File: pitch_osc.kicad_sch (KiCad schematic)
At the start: 32 parts, among them Q1 2N3904, Q2 2N3904, Q3 2N3904, Q4 2N3904, Q5 2N3904

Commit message: Placed in smd and through.
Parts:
- C1, C2, C3, C5, C6, C7, C9: footprint Capacitor_THT:C_Disc_D11.0mm_W5.0mm_P7.50mm -> Capacitor_SMD:C_0805_2012Metric
- C10, C11, C4, C8: footprint Capacitor_THT:CP_Radial_D10.0mm_P3.80mm -> Capacitor_THT:CP_Radial_D5.0mm_P2.50mm
- L5, L6: footprint Inductor_THT:L_Axial_L7.0mm_D3.3mm_P12.70mm_Horizontal_Fastron_MICC -> Inductor_SMD:L_1210_3225Metric
- R1, R10, R11, R12, R13, R14, R2, R3, R4, R5, R6, R7, R8, R9: footprint Resistor_THT:R_Axial_DIN0207_L6.3mm_D2.5mm_P10.16mm_Horizontal -> Resistor_SMD:R_0805_2012Metric
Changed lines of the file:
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@@
       (effects (font (size 1.27 1.27)) (justify left))
     )
-    (property "Footprint" "Resistor_THT:R_Axial_DIN0207_L6.3mm_D2.5mm_P10.16mm_Horizontal" (at 180.086 100.584 90)
+    (property "Footprint" "Resistor_SMD:R_0805_2012Metric" (at 180.086 100.584 90)
       (effects (font (size 1.27 1.27)) hide)
     )
@@
       (effects (font (size 1.27 1.27)) (justify left))
     )
-    (property "Footprint" "Resistor_THT:R_Axial_DIN0207_L6.3mm_D2.5mm_P10.16mm_Horizontal" (at 219.456 104.394 90)
+    (property "Footprint" "Resistor_SMD:R_0805_2012Metric" (at 219.456 104.394 90)
       (effects (font (size 1.27 1.27)) hide)
     )
@@
       (effects (font (size 1.27 1.27)) (justify left))
     )
-    (property "Footprint" "Resistor_THT:R_Axial_DIN0207_L6.3mm_D2.5mm_P10.16mm_Horizontal" (at 105.156 99.314 90)
+    (property "Footprint" "Resistor_SMD:R_0805_2012Metric" (at 105.156 99.314 90)
       (effects (font (size 1.27 1.27)) hide)
     )
@@
       (effects (font (size 1.27 1.27)) (justify left))
     )
-    (property "Footprint" "Resistor_THT:R_Axial_DIN0207_L6.3mm_D2.5mm_P10.16mm_Horizontal" (at 180.086 87.884 90)
+    (property "Footprint" "Resistor_SMD:R_0805_2012Metric" (at 180.086 87.884 90)
       (effects (font (size 1.27 1.27)) hide)
     )
@@
       (effects (font (size 1.27 1.27)) (justify left))
     )
-    (property "Footprint" "Resistor_THT:R_Axial_DIN0207_L6.3mm_D2.5mm_P10.16mm_Horizontal" (at 141.986 101.854 90)
+    (property "Footprint" "Resistor_SMD:R_0805_2012Metric" (at 141.986 101.854 90)
       (effects (font (size 1.27 1.27)) hide)
     )
@@
       (effects (font (size 1.27 1.27)) (justify left))
     )
-    (property "Footprint" "Inductor_THT:L_Axial_L7.0mm_D3.3mm_P12.70mm_Horizontal_Fastron_MICC" (at 147.32 72.39 0)
+    (property "Footprint" "Inductor_SMD:L_1210_3225Metric" (at 147.32 72.39 0)
       (effects (font (size 1.27 1.27)) hide)
     )
@@
       (effects (font (size 1.27 1.27)) (justify left))
     )
-    (property "Footprint" "Resistor_THT:R_Axial_DIN0207_L6.3mm_D2.5mm_P10.16mm_Horizontal" (at 105.156 90.424 90)
+    (property "Footprint" "Resistor_SMD:R_0805_2012Metric" (at 105.156 90.424 90)
       (effects (font (size 1.27 1.27)) hide)
     )
@@
       (effects (font (size 1.27 1.27)) (justify left))
     )
-    (property "Footprint" "Capacitor_THT:CP_Radial_D10.0mm_P3.80mm" (at 201.6252 97.79 0)
+    (property "Footprint" "Capacitor_THT:CP_Radial_D5.0mm_P2.50mm" (at 201.6252 97.79 0)
       (effects (font (size 1.27 1.27)) hide)
     )
@@
       (effects (font (size 1.27 1.27)) (justify right))
     )
-    (property "Footprint" "Resistor_THT:R_Axial_DIN0207_L6.3mm_D2.5mm_P10.16mm_Horizontal" (at 236.474 103.886 90)
+    (property "Footprint" "Resistor_SMD:R_0805_2012Metric" (at 236.474 103.886 90)
       (effects (font (size 1.27 1.27)) hide)
     )
@@
       (effects (font (size 1.27 1.27)) (justify left))
     )
-    (property "Footprint" "Capacitor_THT:CP_Radial_D10.0mm_P3.80mm" (at 191.4652 91.44 0)
+    (property "Footprint" "Capacitor_THT:CP_Radial_D5.0mm_P2.50mm" (at 191.4652 91.44 0)
       (effects (font (size 1.27 1.27)) hide)
     )
@@
       (effects (font (size 1.27 1.27)))
     )
-    (property "Footprint" "Capacitor_THT:C_Disc_D11.0mm_W5.0mm_P7.50mm" (at 161.29 82.8548 0)
+    (property "Footprint" "Capacitor_SMD:C_0805_2012Metric" (at 161.29 82.8548 0)
       (effects (font (size 1.27 1.27)) hide)
     )
@@
       (effects (font (size 1.27 1.27)) (justify left))
     )
-    (property "Footprint" "Resistor_THT:R_Axial_DIN0207_L6.3mm_D2.5mm_P10.16mm_Horizontal" (at 159.766 108.204 90)
+    (property "Footprint" "Resistor_SMD:R_0805_2012Metric" (at 159.766 108.204 90)
       (effects (font (size 1.27 1.27)) hide)
     )
@@
       (effects (font (size 1.27 1.27)) (justify right))
     )
-    (property "Footprint" "Resistor_THT:R_Axial_DIN0207_L6.3mm_D2.5mm_P10.16mm_Horizontal" (at 236.474 92.456 90)
+    (property "Footprint" "Resistor_SMD:R_0805_2012Metric" (at 236.474 92.456 90)
       (effects (font (size 1.27 1.27)) hide)
     )
@@
       (effects (font (size 1.27 1.27)))
     )
-    (property "Footprint" "Capacitor_THT:C_Disc_D11.0mm_W5.0mm_P7.50mm" (at 86.36 89.2048 0)
+    (property "Footprint" "Capacitor_SMD:C_0805_2012Metric" (at 86.36 89.2048 0)
       (effects (font (size 1.27 1.27)) hide)
     )
@@
       (effects (font (size 1.27 1.27)) (justify left))
     )
-    (property "Footprint" "Resistor_THT:R_Axial_DIN0207_L6.3mm_D2.5mm_P10.16mm_Horizontal" (at 50.546 112.014 90)
+    (property "Footprint" "Resistor_SMD:R_0805_2012Metric" (at 50.546 112.014 90)
       (effects (font (size 1.27 1.27)) hide)
     )
@@
       (effects (font (size 1.27 1.27)) (justify right))
     )
-    (property "Footprint" "Resistor_THT:R_Axial_DIN0207_L6.3mm_D2.5mm_P10.16mm_Horizontal" (at 246.634 103.886 90)
+    (property "Footprint" "Resistor_SMD:R_0805_2012Metric" (at 246.634 103.886 90)
       (effects (font (size 1.27 1.27)) hide)
     )
@@
       (effects (font (size 1.27 1.27)) (justify left))
     )
-    (property "Footprint" "Capacitor_THT:C_Disc_D11.0mm_W5.0mm_P7.50mm" (at 39.0652 104.14 0)
+    (property "Footprint" "Capacitor_SMD:C_0805_2012Metric" (at 39.0652 104.14 0)
       (effects (font (size 1.27 1.27)) hide)
     )
@@
       (effects (font (size 1.27 1.27)) (justify left))
     )
-    (property "Footprint" "Capacitor_THT:CP_Radial_D10.0mm_P3.80mm" (at 115.2652 96.52 0)
+    (property "Footprint" "Capacitor_THT:CP_Radial_D5.0mm_P2.50mm" (at 115.2652 96.52 0)
       (effects (font (size 1.27 1.27)) hide)
     )
@@
       (effects (font (size 1.27 1.27)) (justify left))
     )
-    (property "Footprint" "Capacitor_THT:C_Disc_D11.0mm_W5.0mm_P7.50mm" (at 139.3952 76.2 0)
+    (property "Footprint" "Capacitor_SMD:C_0805_2012Metric" (at 139.3952 76.2 0)
       (effects (font (size 1.27 1.27)) hide)
     )
@@
       (effects (font (size 1.27 1.27)) (justify left))
     )
-    (property "Footprint" "Capacitor_THT:C_Disc_D11.0mm_W5.0mm_P7.50mm" (at 134.3152 96.52 0)
+    (property "Footprint" "Capacitor_SMD:C_0805_2012Metric" (at 134.3152 96.52 0)
       (effects (font (size 1.27 1.27)) hide)
     )
@@
       (effects (font (size 1.27 1.27)) (justify left))
     )
-    (property "Footprint" "Resistor_THT:R_Axial_DIN0207_L6.3mm_D2.5mm_P10.16mm_Horizontal" (at 213.106 103.124 90)
+    (property "Footprint" "Resistor_SMD:R_0805_2012Metric" (at 213.106 103.124 90)
       (effects (font (size 1.27 1.27)) hide)
     )
@@
       (effects (font (size 1.27 1.27)) (justify right))
     )
-    (property "Footprint" "Capacitor_THT:C_Disc_D11.0mm_W5.0mm_P7.50mm" (at 239.0648 73.66 0)
+    (property "Footprint" "Capacitor_SMD:C_0805_2012Metric" (at 239.0648 73.66 0)
       (effects (font (size 1.27 1.27)) hide)
     )
@@
       (effects (font (size 1.27 1.27)) (justify left))
     )
-    (property "Footprint" "Capacitor_THT:C_Disc_D11.0mm_W5.0mm_P7.50mm" (at 56.8452 85.09 0)
+    (property "Footprint" "Capacitor_SMD:C_0805_2012Metric" (at 56.8452 85.09 0)
       (effects (font (size 1.27 1.27)) hide)
     )
@@
       (effects (font (size 1.27 1.27)) (justify left))
     )
-    (property "Footprint" "Resistor_THT:R_Axial_DIN0207_L6.3mm_D2.5mm_P10.16mm_Horizontal" (at 75.946 110.744 90)
+    (property "Footprint" "Resistor_SMD:R_0805_2012Metric" (at 75.946 110.744 90)
       (effects (font (size 1.27 1.27)) hide)
     )
@@
       (effects (font (size 1.27 1.27)))
     )
-    (property "Footprint" "Capacitor_THT:CP_Radial_D10.0mm_P3.80mm" (at 223.52 98.7552 0)
+    (property "Footprint" "Capacitor_THT:CP_Radial_D5.0mm_P2.50mm" (at 223.52 98.7552 0)
       (effects (font (size 1.27 1.27)) hide)
     )
@@
       (effects (font (size 1.27 1.27)))
     )
-    (property "Footprint" "Resistor_THT:R_Axial_DIN0207_L6.3mm_D2.5mm_P10.16mm_Horizontal" (at 230.124 85.344 90)
+    (property "Footprint" "Resistor_SMD:R_0805_2012Metric" (at 230.124 85.344 90)
       (effects (font (size 1.27 1.27)) hide)
     )
@@
       (effects (font (size 1.27 1.27)) (justify left))
     )
-    (property "Footprint" "Inductor_THT:L_Axial_L7.0mm_D3.3mm_P12.70mm_Horizontal_Fastron_MICC" (at 68.58 81.28 0)
-      (effects (font (size 1.27 1.27)) hide)
-    )
+    (property "Footprint" "Inductor_SMD:L_1210_3225Metric" (at 68.58 81.28 0)
+      (effects (font (size 1.27 1.27)) hide)
+    )

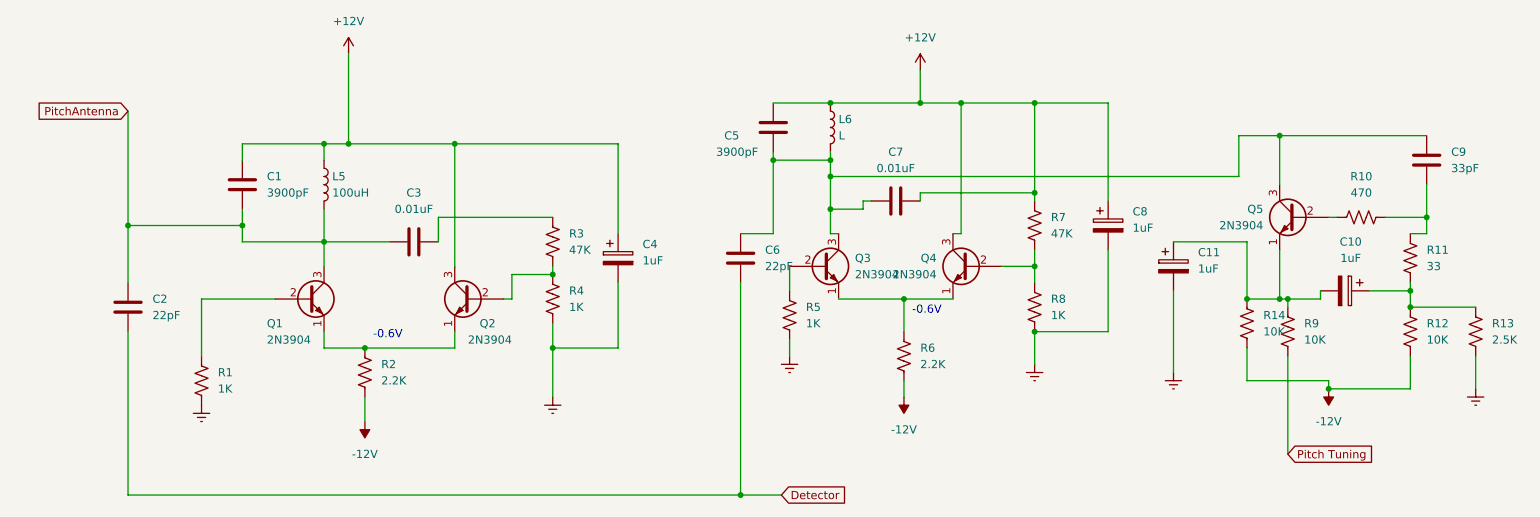
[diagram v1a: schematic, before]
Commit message: Layout cleanup for smd and through
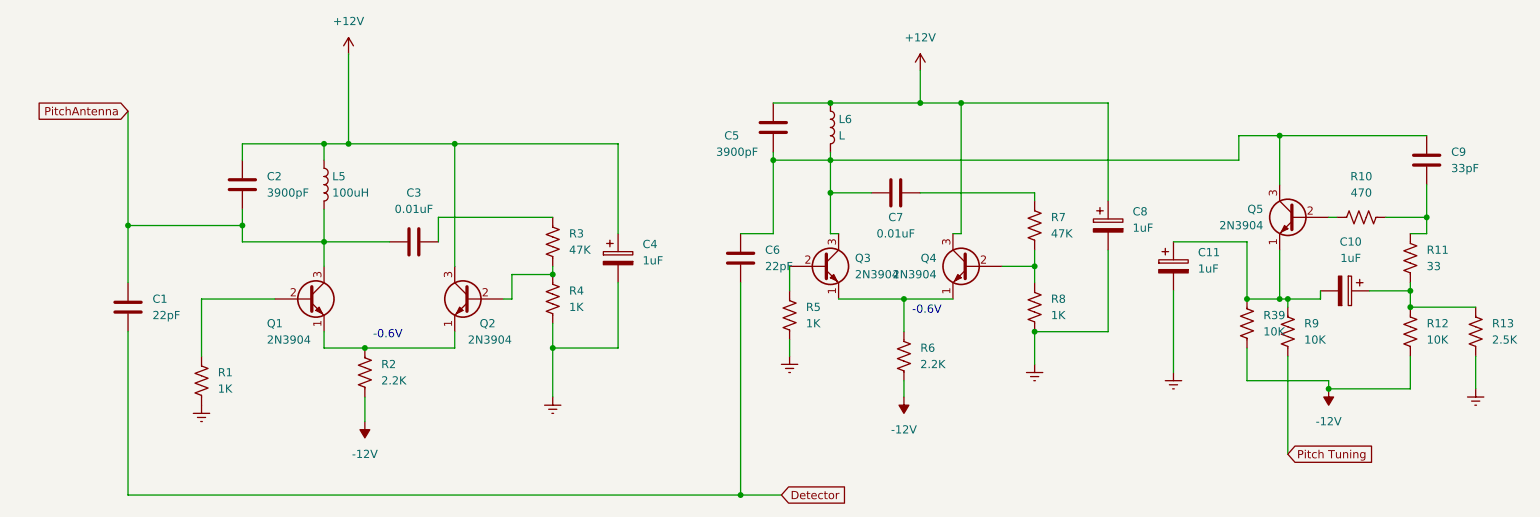
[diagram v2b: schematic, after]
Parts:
- renumbered C2 to C1, C1 to C2, R14 to R39
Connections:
- net +12V: no longer C7.2, R7.1
- new net: C7.2, R7.1
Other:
- moved on the sheet: C7
